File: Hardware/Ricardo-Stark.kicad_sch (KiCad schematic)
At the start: 48 parts, among them J1 RBUS, J11 Conn_01x08_Socket, J5 Conn_01x03_Socket, U1 ESP32-S3, U14 PCA9534RGVR, Y1 R940000171

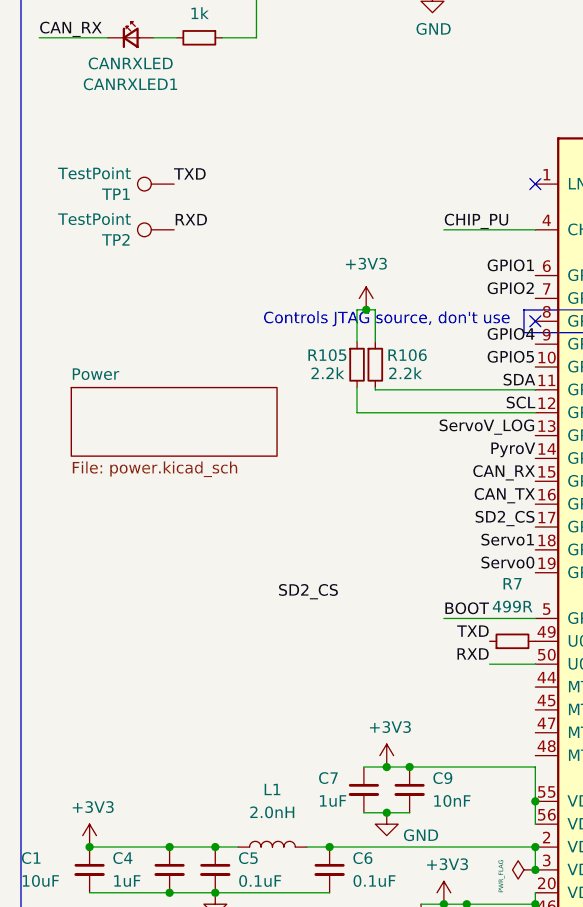
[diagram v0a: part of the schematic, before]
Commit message: Updated Silkcreen and test points
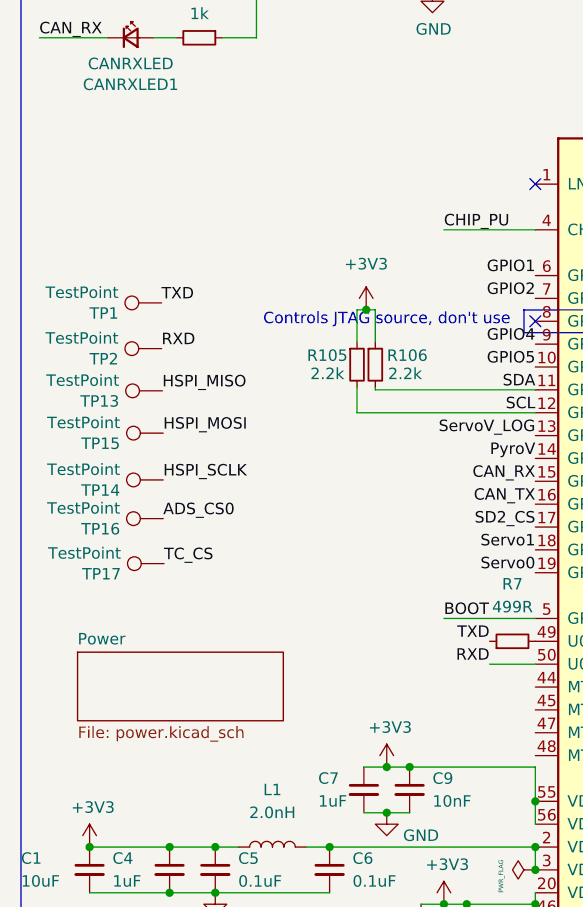
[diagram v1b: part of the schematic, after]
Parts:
- added TP13, TP14, TP15, TP16, TP17: TestPoint, TestPoint:TestPoint_Pad_D1.0mm, symbol Connector:TestPoint
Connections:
- net ADS_CS0: now also TP16.1
- net HSPI_MISO: now also TP13.1
- net HSPI_MOSI: now also TP15.1
- net HSPI_SCLK: now also TP14.1
- net TC_CS: now also TP17.1
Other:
- moved on the sheet: TP1, TP2

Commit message: v2 Ready for Review
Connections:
- net +3V3: now also R105.2, R106.2; no longer R105.1, R106.1
- net SCL: now also R105.1; no longer R105.2
- net SDA: now also R106.1; no longer R106.2, U1.11 (GPIO6/ADC1_CH5)
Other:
- moved on the sheet: C36, C90, D7, J11, J5, R105, R106, U14

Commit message: Most Review Changes
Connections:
- net SCL: now also D7.7 (K/A_6), J5.3 (Pin_3), R106.1, U1.11 (GPIO6/ADC1_CH5); no longer D7.4 (K/A_3), J5.2 (Pin_2), R105.1, U1.12 (GPIO7/ADC1_CH6)
- net SDA: now also D7.4 (K/A_3), J5.2 (Pin_2), R105.1, U1.12 (GPIO7/ADC1_CH6); no longer D7.7 (K/A_6), J5.3 (Pin_3), R106.1
- no-connect marks 14 -> 22
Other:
- sheet microSD ports: added none; removed SD_Pow
- note removed: "This is the bare minimum required for a board in the Ricardo ecosystem. Please ask before changing or removing anything in this box."
- moved on the sheet: C36, C90, D7, U14

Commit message: Remaining Review Changes
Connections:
- net PyroV is gone; now on net Nuke 1: U1.14 (GPIO9/ADC1_CH8)
- net Nuke 1: no longer U14.4 (P2)
- net SD1_CS: now also U1.24 (GPIO18/ADC2_CH7/DAC_1); no longer U1.21 (GPIO15/ADC2_CH4/XTAL_32K_P)
- net VSPI_MISO: now also U1.21 (GPIO15/ADC2_CH4/XTAL_32K_P); no longer U1.24 (GPIO18/ADC2_CH7/DAC_1)
- net VSPI_MOSI: now also U1.23 (GPIO17/ADC2_CH6/DAC_2); no longer U1.22 (GPIO16/ADC2_CH5/XTAL_32K_N)
- net VSPI_SCLK: now also U1.22 (GPIO16/ADC2_CH5/XTAL_32K_N); no longer U1.23 (GPIO17/ADC2_CH6/DAC_2)
- no-connect marks 22 -> 23
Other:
- sheet Pyro ports: added none; removed PyroVMON
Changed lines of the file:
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@@
 	)
 	(no_connect
+		(at 190.754 145.796)
+	)
+	(no_connect
 		(at 135.89 87.63)
 	)
@@
 	)
 	(label "VSPI_MISO"
-		(at 135.89 69.85 0)
+		(at 135.89 128.27 0)
 		(effects
 			(font
@@
 		)
 	)
-	(label "PyroV"
-		(at 69.85 92.71 180)
-		(effects
-			(font
-				(size 1.27 1.27)
-			)
-			(justify right bottom)
-		)
-	)
 	(label "GPIO1"
 		(at 274.69 107.52 180)
@@
 	)
 	(label "SD1_CS"
-		(at 135.89 128.27 0)
+		(at 135.89 69.85 0)
 		(effects
 			(font
@@
 	)
 	(label "Nuke 1"
-		(at 190.754 145.796 180)
+		(at 69.85 92.71 180)
 		(effects
 			(font
@@
 	)
 	(label "VSPI_MOSI"
-		(at 135.89 130.81 0)
+		(at 135.89 72.39 0)
 		(effects
 			(font
@@
 		)
 	)
-	(label "PyroV"
-		(at 219 97.502 0)
-		(effects
-			(font
-				(size 1.27 1.27)
-			)
-			(justify left bottom)
-		)
-	)
 	(label "CAN_RX"
 		(at 115.57 182.88 0)
@@
 	)
 	(label "VSPI_SCLK"
-		(at 135.89 72.39 0)
+		(at 135.89 130.81 0)
 		(effects
 			(font
@@
 			(effects
 				(font
-					(size 1.27 1.27)
-				)
-				(justify right)
-			)
-		)
-		(pin "PyroVMON" output
-			(at 219 97.502 0)
-			(effects
-				(font

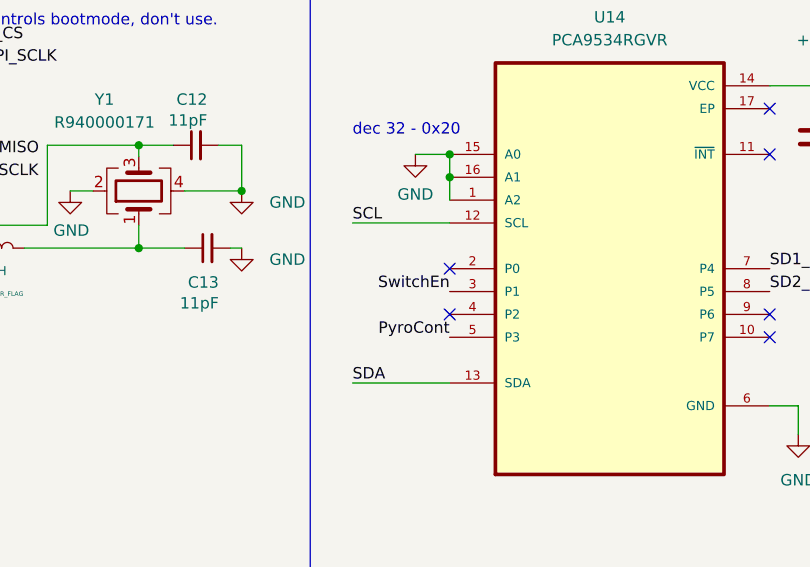
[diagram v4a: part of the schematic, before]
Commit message: Replaced PicoClasp with nanofits
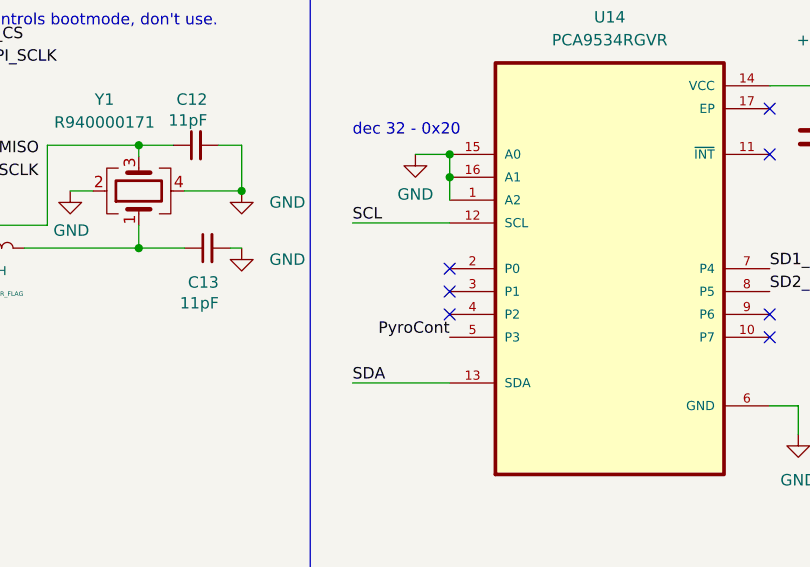
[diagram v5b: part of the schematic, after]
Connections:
- net SwitchEn: no longer U14.3 (P1)
- no-connect marks 23 -> 24
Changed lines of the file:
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@@
+	)
+	(no_connect
+		(at 190.754 143.256)
 	)
 	(no_connect
@@
 		)
 	)
-	(label "SwitchEn"
-		(at 190.754 143.256 180)
-		(effects
-			(font
-				(size 1.27 1.27)
-			)
-			(justify right bottom)
-		)
-	)

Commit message: Solenoid Feature and minor changes
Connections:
- net Sol1Cont: now reaches U14.10 (P7)
- net Nuke 3: now reaches U14.2 (P0)
- net Nuke 2: now reaches U14.3 (P1)
- net Sol0Cont: now reaches U14.4 (P2)
- no-connect marks 24 -> 20
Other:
- sheet Pyro ports: added Cont2, Cont3, Nuke 2, Nuke 3; removed EN
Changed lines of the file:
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@@
 	)
 	(no_connect
-		(at 190.754 143.256)
-	)
-	(no_connect
 		(at 69.85 120.65)
 	)
@@
 	)
 	(no_connect
-		(at 190.754 140.716)
-	)
-	(no_connect
 		(at 69.85 77.47)
 	)
@@
 	)
 	(no_connect
-		(at 226.314 148.336)
-	)
-	(no_connect
-		(at 190.754 145.796)
-	)
-	(no_connect
 		(at 135.89 87.63)
 	)
@@
 	(wire
 		(pts
+			(xy 176.53 99.822) (xy 186.182 99.822)
+		)
+		(stroke
+			(width 0)
+			(type default)
+		)
+	)
+	(wire
+		(pts
 			(xy 16.51 191.77) (xy 20.32 191.77)
 		)
@@
 	(wire
 		(pts
+			(xy 179.832 143.256) (xy 190.754 143.256)
+		)
+		(stroke
+			(width 0)
+			(type default)
+		)
+	)
+	(wire
+		(pts
 			(xy 267.97 33.02) (xy 262.89 33.02)
 		)
@@
 	(wire
 		(pts
+			(xy 179.832 145.796) (xy 190.754 145.796)
+		)
+		(stroke
+			(width 0)
+			(type default)
+		)
+	)
+	(wire
+		(pts
 			(xy 68.58 165.1) (xy 63.5 165.1)
 		)
@@
 	(wire
 		(pts
+			(xy 220.726 103.886) (xy 218.948 103.886)
+		)
+		(stroke
+			(width 0)
+			(type default)
+		)
+	)
+	(wire
+		(pts
 			(xy 190.754 128.016) (xy 190.754 130.556)
 		)
@@
 		)
 	)
+	(wire
+		(pts
+			(xy 176.53 94.996) (xy 186.182 94.996)
+		)
+		(stroke
+			(width 0)
+			(type default)
+		)
+	)
 	(polyline
 		(pts
@@
 	(wire
 		(pts
-			(xy 177.09 104.614) (xy 186.234 104.614)
+			(xy 176.53 102.108) (xy 186.182 102.108)
 		)
 		(stroke
@@
 	(wire
 		(pts
+			(xy 220.726 106.68) (xy 218.948 106.68)
+		)
+		(stroke
+			(width 0)
+			(type default)
+		)
+	)
+	(wire
+		(pts
+			(xy 188.468 148.336) (xy 190.754 148.336)
+		)
+		(stroke
+			(width 0)
+			(type default)
+		)
+	)
+	(wire
+		(pts
 			(xy 52.8 85.1) (xy 53.96 85.1)
 		)
@@
 	(wire
 		(pts
+			(xy 176.53 106.68) (xy 186.182 106.68)
+		)
+		(stroke
+			(width 0)
+			(type default)
+		)
+	)
+	(wire
+		(pts
 			(xy 52.8 86.2) (xy 52.8 87.6)
 		)
@@
 		)
 	)
+	(wire
+		(pts
+			(xy 179.832 140.716) (xy 190.754 140.716)
+		)
+		(stroke
+			(width 0)
+			(type default)
+		)
+	)
 	(polyline
 		(pts
@@
 	(wire
 		(pts
+			(xy 176.53 104.394) (xy 186.182 104.394)
+		)
+		(stroke
+			(width 0)
+			(type default)
+		)
+	)
+	(wire
+		(pts
 			(xy 55.88 165.1) (xy 63.5 165.1)
 		)
@@
 	(wire
 		(pts
+			(xy 176.53 97.282) (xy 186.182 97.282)
+		)
+		(stroke
+			(width 0)
+			(type default)
+		)
+	)
+	(wire
+		(pts
 			(xy 34.29 170.18) (xy 34.29 165.1)
 		)
@@
 	(wire
 		(pts
-			(xy 176.836 100.804) (xy 186.234 100.804)
-		)
-		(stroke
-			(width 0)
-			(type default)
-		)
-	)
-	(wire
-		(pts
 			(xy 39.37 33.274) (xy 38.862 33.274)
 		)
@@
 		)
 	)
-	(label "SwitchEn"
-		(at 219 101.058 0)
-		(effects
-			(font
-				(size 1.27 1.27)
-			)
-			(justify left bottom)
-		)
-	)
 	(label "Nuke 1"
-		(at 177.09 104.614 0)
+		(at 176.53 102.108 0)
 		(effects
 			(font
@@
 		)
 	)
+	(label "Sol1Cont"
+		(at 176.53 99.822 0)
+		(effects
+			(font
+				(size 1.27 1.27)
+			)
+			(justify left bottom)
+		)
+	)
 	(label "GPIO2"
 		(at 278.13 143.256 0)
@@
 	)
 	(label "SCL"
-		(at 219 104.614 0)
+		(at 220.726 103.886 0)
 		(effects
 			(font
@@
 		)
 	)
+	(label "Sol0Cont"
+		(at 176.53 97.282 0)
+		(effects
+			(font
+				(size 1.27 1.27)
+			)
+			(justify left bottom)
+		)
+	)
 	(label "SD2_DET"
 		(at 214.6 50.752 0)
@@
 	)
 	(label "PyroCont"
-		(at 176.836 100.804 0)
+		(at 176.53 94.996 0)
 		(effects
 			(font
@@
 	)
 	(label "PyroCont"
-		(at 190.754 148.336 180)
+		(at 188.468 148.336 180)
 		(effects
 			(font
@@
 		)
 	)
+	(label "Sol1Cont"
+		(at 226.314 148.336 0)
+		(effects
+			(font
+				(size 1.27 1.27)
+			)
+			(justify left bottom)
+		)
+	)
+	(label "Nuke 3"
+		(at 176.53 106.68 0)
+		(effects
+			(font
+				(size 1.27 1.27)
+			)
+			(justify left bottom)
+		)
+	)
 	(label "CAN-"
 		(at 115.57 25.4 270)
@@
 		)
 	)
+	(label "Nuke 2"
+		(at 179.832 143.256 0)
+		(effects
+			(font
+				(size 1.27 1.27)
+			)
+			(justify left bottom)
+		)
+	)
 	(label "SD1_DET"
 		(at 190.47 50.752 180)
@@
 		)
 	)
+	(label "Sol0Cont"
+		(at 179.832 145.796 0)
+		(effects
+			(font
+				(size 1.27 1.27)
+			)
+			(justify left bottom)
+		)
+	)
 	(label "BOOT"
 		(at 68.58 165.1 180)
@@
 		)
 	)
+	(label "Nuke 2"
+		(at 176.53 104.394 0)
+		(effects
+			(font
+				(size 1.27 1.27)
+			)
+			(justify left bottom)
+		)
+	)
 	(label "VSPI_MOSI"
 		(at 135.89 72.39 0)
@@
 		)
 	)
+	(label "Nuke 3"
+		(at 179.832 140.716 0)
+		(effects
+			(font
+				(size 1.27 1.27)
+			)
+			(justify left bottom)
+		)
+	)
 	(label "SDA"
-		(at 219 106.9 0)
+		(at 220.726 106.68 0)
 		(effects
 			(font
@@
 	)
 	(sheet
-		(at 186.234 93.438)
+		(at 186.182 93.438)
 		(size 32.766 14.732)
 		(exclude_from_sim no)
@@
 		)
 		(property "Sheetname" "Pyro"
-			(at 186.234 92.7264 0)
+			(at 186.182 92.7264 0)
 			(effects
 				(font
@@
 		)
 		(property "Sheetfile" "Pyro.kicad_sch"
-			(at 186.234 108.7546 0)
+			(at 186.182 108.7546 0)
 			(effects
 				(font
@@
 		)
 		(pin "Cont1" output
-			(at 186.234 100.804 180)
+			(at 186.182 94.996 180)
 			(effects
 				(font
@@
 		)
 		(pin "Nuke 1" input
-			(at 186.234 104.614 180)
+			(at 186.182 102.108 180)
 			(effects
 				(font
@@
 			)
 		)
-		(pin "EN" input
-			(at 219 101.058 0)
+		(pin "SCL" bidirectional
+			(at 218.948 103.886 0)
 			(effects
 				(font
@@
 			)
 		)
-		(pin "SCL" bidirectional
-			(at 219 104.614 0)
+		(pin "SDA" bidirectional
+			(at 218.948 106.68 0)
 			(effects
 				(font
@@
 			)
 		)
-		(pin "SDA" bidirectional
-			(at 219 106.9 0)
+		(pin "Cont2" output
+			(at 186.182 97.282 180)
 			(effects
 				(font
 					(size 1.27 1.27)
 				)
-				(justify right)
+				(justify left)
+			)
+		)
+		(pin "Cont3" output
+			(at 186.182 99.822 180)
+			(effects
+				(font
+					(size 1.27 1.27)
+				)
+				(justify left)
+			)
+		)
+		(pin "Nuke 2" input
+			(at 186.182 104.394 180)
+			(effects
+				(font
+					(size 1.27 1.27)
+				)
+				(justify left)
+			)
+		)
+		(pin "Nuke 3" input
+			(at 186.182 106.68 180)
+			(effects
+				(font
+					(size 1.27 1.27)
+				)
+				(justify left)
 			)
 		)

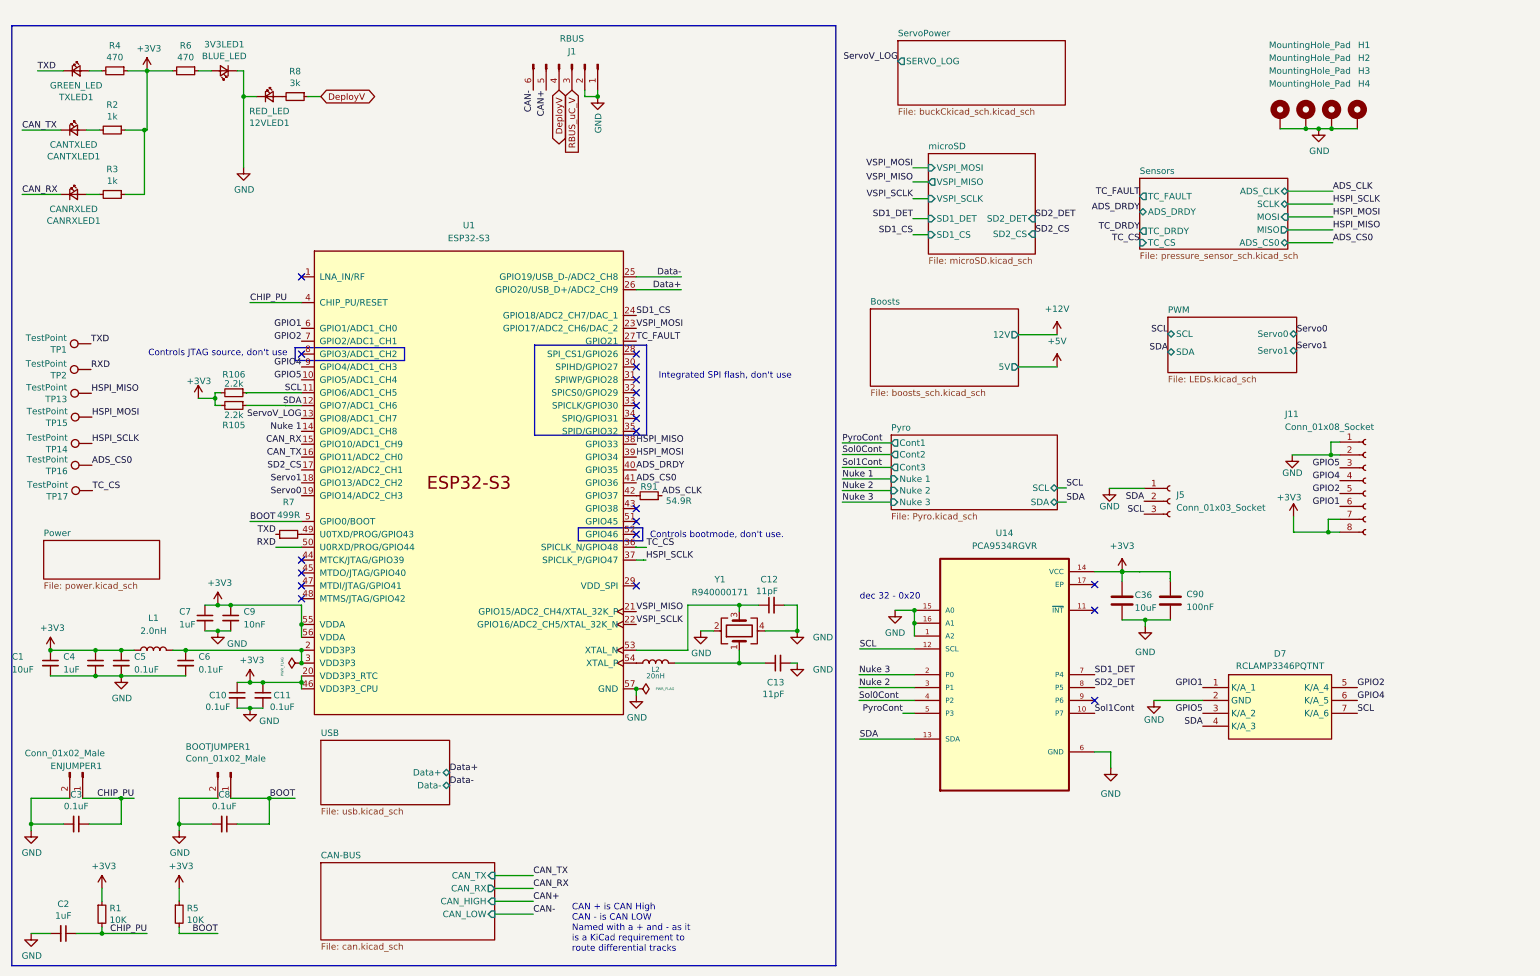
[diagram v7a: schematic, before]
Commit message: schematic reformatting and bom consolidation
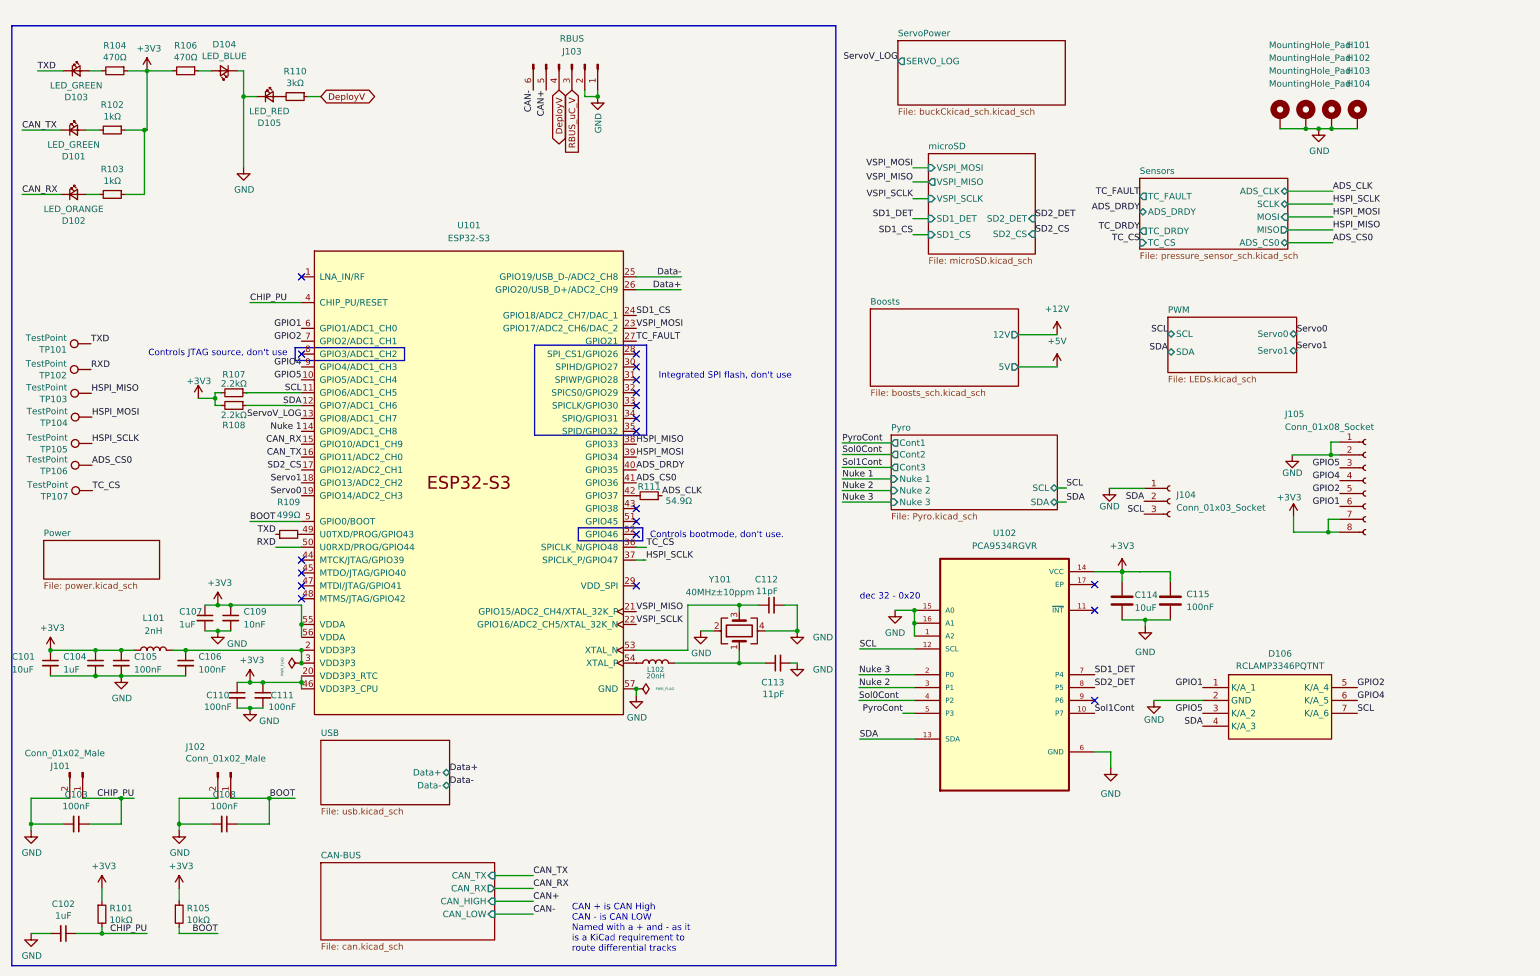
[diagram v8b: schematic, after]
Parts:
- C103: renamed from C3; value 0.1uF -> 100nF
- C105: renamed from C5; value 0.1uF -> 100nF
- C106: renamed from C6; value 0.1uF -> 100nF
- C108: renamed from C8; value 0.1uF -> 100nF
- C110: renamed from C10; value 0.1uF -> 100nF
- C111: renamed from C11; value 0.1uF -> 100nF
- D101: renamed from CANTXLED1; value CANTXLED -> LED_GREEN
- D102: renamed from CANRXLED1; value CANRXLED -> LED_ORANGE
- D103: renamed from TXLED1; value GREEN_LED -> LED_GREEN; footprint Resistor_SMD:R_0402_1005Metric -> LED_SMD:LED_0402_1005Metric
- D104: renamed from 3V3LED1; value BLUE_LED -> LED_BLUE; footprint Resistor_SMD:R_0402_1005Metric -> LED_SMD:LED_0402_1005Metric
- D105: renamed from 12VLED1; value RED_LED -> LED_RED; footprint Resistor_SMD:R_0402_1005Metric -> LED_SMD:LED_0402_1005Metric
- H101: renamed from H1; now left out of the parts list
- H102: renamed from H2; now left out of the parts list
- H103: renamed from H3; now left out of the parts list
- H104: renamed from H4; now left out of the parts list
- L101: renamed from L1; value 2.0nH -> 2nH
- R101: renamed from R1; value 10K -> 10kΩ
- R102: renamed from R2; value 1k -> 1kΩ
- R103: renamed from R3; value 1k -> 1kΩ
- R104: renamed from R4; value 470 -> 470Ω
- R105: renamed from R5; value 10K -> 10kΩ
- R106: renamed from R6; value 470 -> 470Ω
- R107: renamed from R106; value 2.2k -> 2.2kΩ
- R108: renamed from R105; value 2.2k -> 2.2kΩ
- R109: renamed from R7; value 499R -> 499Ω
- R110: renamed from R8; value 3k -> 3kΩ
- R111: renamed from R91; value 54.9R -> 54.9Ω
- TP101: renamed from TP1; now left out of the parts list
- TP102: renamed from TP2; now left out of the parts list
- TP103: renamed from TP13; now left out of the parts list
- TP104: renamed from TP15; now left out of the parts list
- TP105: renamed from TP14; now left out of the parts list
- TP106: renamed from TP16; now left out of the parts list
- TP107: renamed from TP17; now left out of the parts list
- Y101: renamed from Y1; value R940000171 -> 40MHz±10ppm; MPN (none) -> R940000171
- renumbered C1 to C101, C2 to C102, C4 to C104, C7 to C107, C9 to C109, C12 to C112, C13 to C113, C36 to C114, C90 to C115, D7 to D106, ENJUMPER1 to J101, BOOTJUMPER1 to J102, J1 to J103, J5 to J104, J11 to J105, L2 to L102, U1 to U101, U14 to U102
